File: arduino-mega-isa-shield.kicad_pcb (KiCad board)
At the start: 2 copper layers, 144.7 x 80.3 mm, 11 parts, among them J1 395-098-520-350, J2 JST VH 1x6, U1 ICS501, Y1 3.579545MHZ

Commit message: Move power connector back so it doesn't hang off the board
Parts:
- moved C3 6.88 mm to (95.6, 97.3)
- moved J2 3.43 mm to (85.2, 81.8)
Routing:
- net -12V: track 98.2 -> 115.5 mm
- net +12V: track 106.0 -> 117.5 mm
- net +5V: track 403.8 -> 414.1 mm
- net GND: track 491.4 -> 499.1 mm
- net /OSC_14M318: track 153.9 -> 154.5 mm
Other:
- outline, holes or cut-outs redrawn

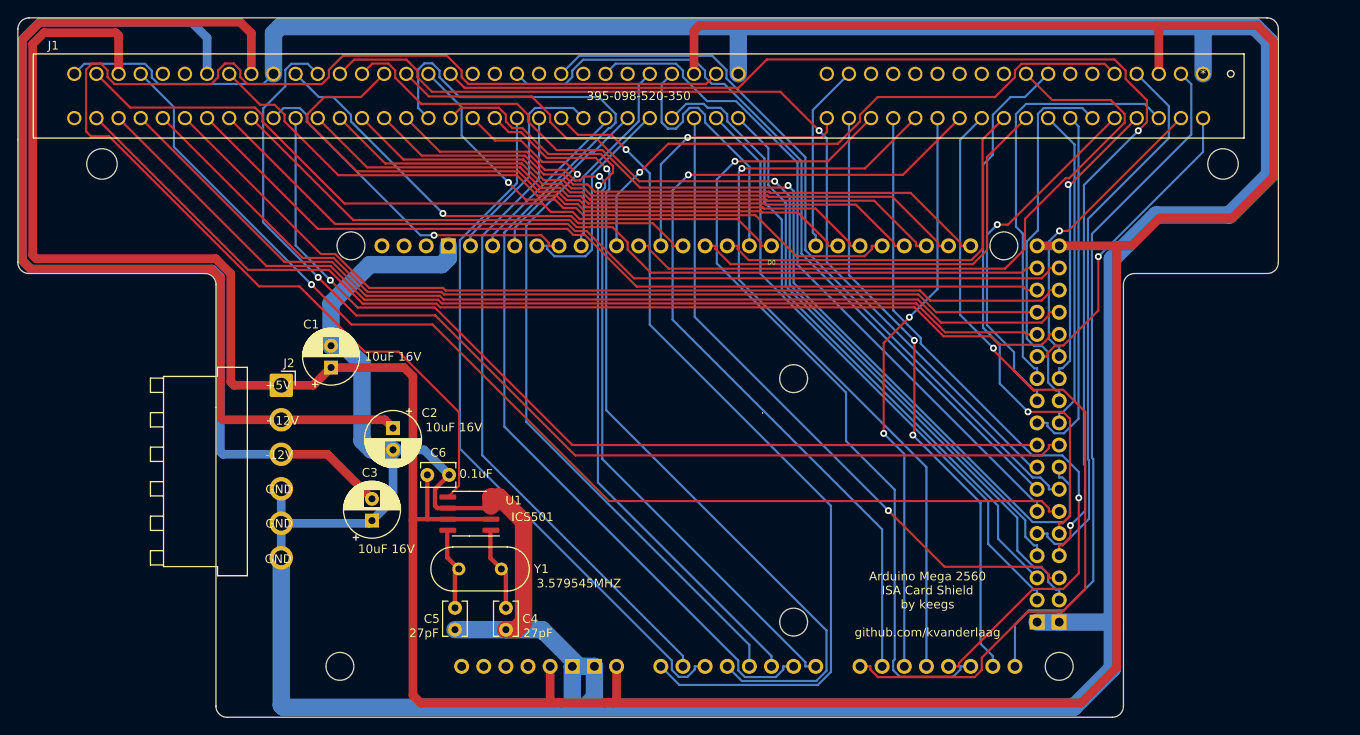
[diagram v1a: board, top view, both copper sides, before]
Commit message: Rework board
lmao the ISA connector pinout was flipped
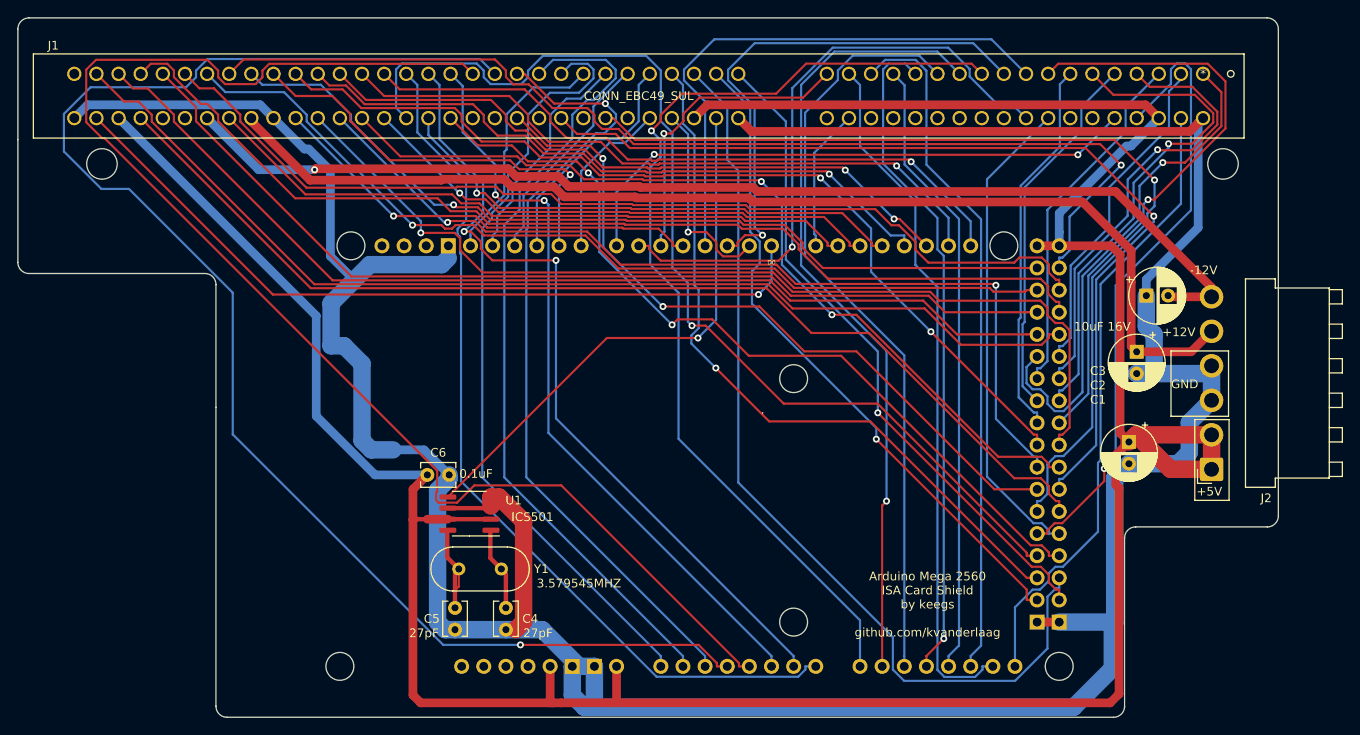
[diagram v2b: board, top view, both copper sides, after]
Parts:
- J1: value 395-098-520-350 -> CONN_EBC49_SUL
- moved J2 107.2 mm to (192.0, 91.4), turned to 90 degrees
- moved C3 92.5 mm to (184.5, 71.5), turned to 0 degrees
- moved C1 92.0 mm to (182.5, 88.3), turned to -90 degrees
- moved C2 85.8 mm to (183.4, 77.9)
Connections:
- J2 pad 2: +12V -> +5V
- J2 pad 3: -12V -> GND
- J2 pad 5: GND -> +12V
- J2 pad 6: GND -> -12V
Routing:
- net GND: track 499.1 -> 377.3 mm
- net /OSC_14M318: track 154.5 -> 62.4 mm, vias 0 -> 1
- net /A12: track 84.2 -> 160.3 mm, vias 1 -> 0
- net /A11: track 96.2 -> 167.9 mm
- net +5V: track 414.1 -> 343.8 mm
- net /DRQ1: track 141.2 -> 96.0 mm
- net /PC0: track 37.2 -> 69.2 mm, vias 0 -> 1
- net /IRQ3: track 79.3 -> 110.3 mm, vias 0 -> 1
- net /A2: track 77.3 -> 106.5 mm, vias 1 -> 0
- net /A14: track 119.7 -> 91.9 mm, vias 0 -> 2
- net /IRQ5: track 85.6 -> 108.7 mm, vias 0 -> 1
- net /PC7: track 36.5 -> 58.2 mm
- net /LA19: track 66.5 -> 87.7 mm, vias 2 -> 0
- net /D1: track 103.6 -> 123.9 mm, vias 0 -> 1
- net /PH1: track 81.1 -> 60.9 mm, vias 0 -> 1
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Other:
- outline, holes or cut-outs redrawn
